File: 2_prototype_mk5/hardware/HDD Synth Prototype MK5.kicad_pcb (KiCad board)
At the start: 2 copper layers, 100.3 x 69.9 mm, 40 parts, among them J1 Micro_SD_Card, J6 171825-4, J7 Conn_01x04_Pin, J8 Conn_01x05, Q1 2N7002, U1 MAX98357A, U2 Optocoupler_DC_PhotoNPN_AKEC

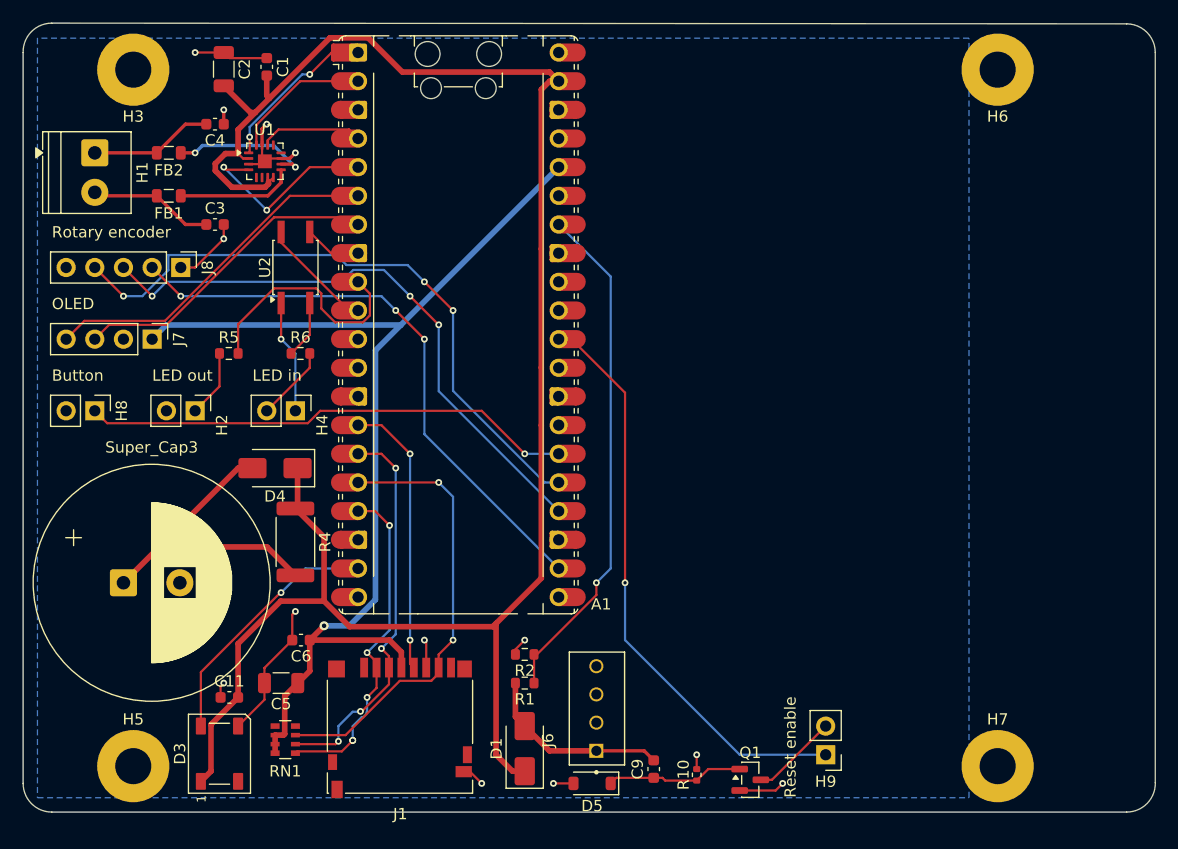
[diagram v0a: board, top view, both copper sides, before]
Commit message: MKV - SATA connector and wiring complete
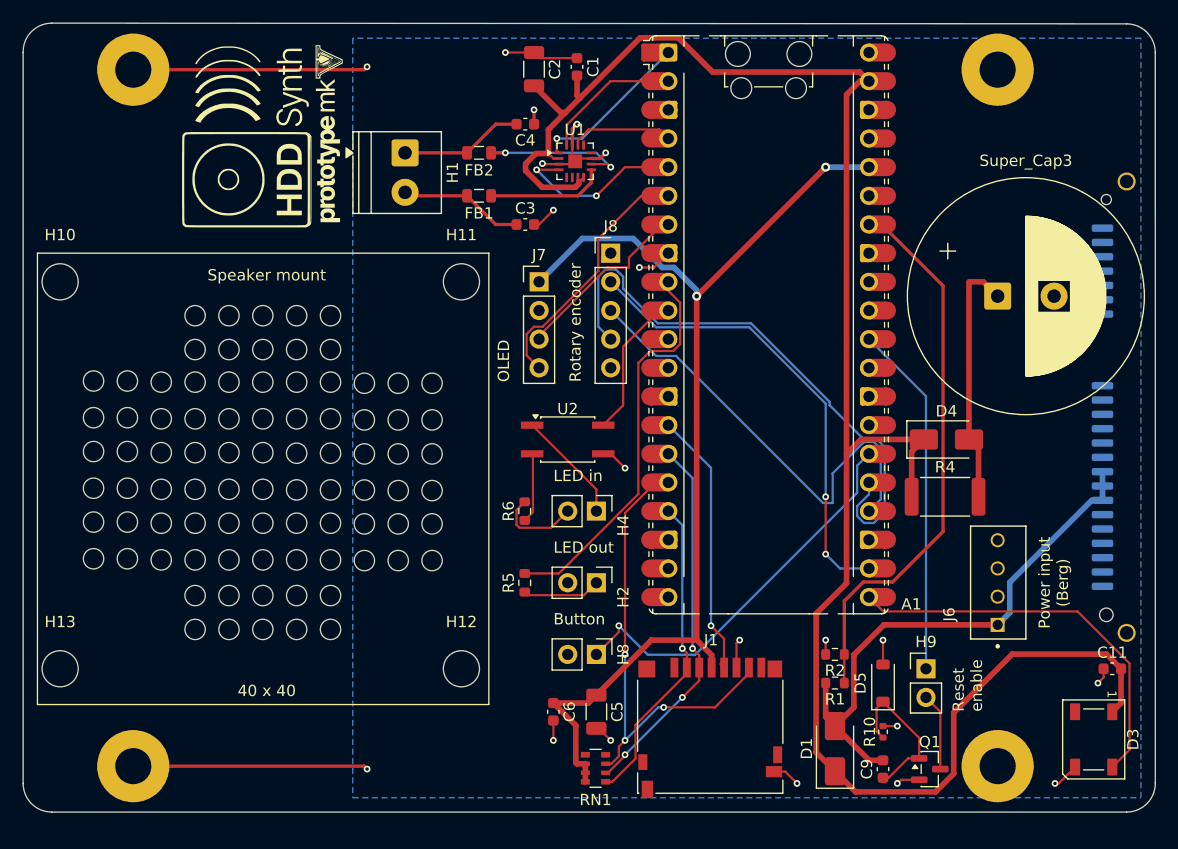
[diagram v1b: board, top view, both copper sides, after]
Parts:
- removed the G*** at (155.2, 79.3)
- added  : LOGO, HDDSyncMKIII:MHDDLA_Sound_40mm, B.Cu at (94.0, 62.1)
- added G***: LOGO, Custom:HDDSynthLogoMKV_15mm, F.Cu at (95.2, 55.9)
- added G***: LOGO, HDDSyncMKIII:MHDDLA_GB_40mm, B.Cu at (119.4, 104.1)
- added H10: MountingHole, MountingHole:MountingHole_3.2mm_M3, F.Cu at (76.9, 69.8)
- added H11: MountingHole, MountingHole:MountingHole_3.2mm_M3, F.Cu at (112.5, 69.8)
- added H12: MountingHole, MountingHole:MountingHole_3.2mm_M3, F.Cu at (112.5, 104.1)
- added H13: MountingHole, MountingHole:MountingHole_3.2mm_M3, F.Cu at (76.9, 104.1)
- added J2: SATA00102253A, Connector_SATA_SAS:SATA_Amphenol_10029364-001LF_Horizontal, B.Cu at (170.3, 81.0)
- moved Super_Cap3 81.5 mm to (160.0, 71.1)
- moved C11 78.3 mm to (170.2, 104.1)
- moved D3 77.5 mm to (168.5, 110.4), turned to -90 degrees
- moved D4 59.6 mm to (155.5, 83.8), turned to 0 degrees
- moved R4 57.7 mm to (155.4, 88.9), turned to 0 degrees
- moved H8 49.4 mm to (124.5, 102.9)
- moved H2 38.7 mm to (124.5, 96.5)
- moved J8 38.1 mm to (125.7, 67.3), turned to 0 degrees
- moved J6 37.3 mm to (160.0, 100.2)
- moved J7 34.7 mm to (119.4, 69.8), turned to 0 degrees
- moved R5 33.2 mm to (118.1, 96.5), turned to 90 degrees
- moved U2 28.5 mm to (121.9, 83.8), turned to 0 degrees
- moved H4 28.1 mm to (124.5, 90.2)
- moved C5 28.1 mm to (124.5, 108.0), turned to -90 degrees
- moved RN1 27.6 mm to (124.4, 113.0)
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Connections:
- A1 pad 19: /RGB LED/RGB_DATA -> unconnected-(A1-GPIO14-Pad19)_1
- A1 pad 21: unconnected-(A1-GPIO16-Pad21)_1 -> /RGB LED/RGB_DATA
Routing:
- net GND: track 54.1 -> 86.0 mm, vias 13 -> 20
- net +5V: track 16.8 -> 48.5 mm
- net /Reset/PICO_RUN: track 51.8 -> 31.3 mm, vias 1 -> 0
- net /HDD_LED_OUT: track 21.3 -> 35.3 mm
- net /RGB LED/RGB_DATA: track 22.5 -> 35.3 mm, vias 1 -> 0
- net /Rotary encoder/ENC_B: track 52.9 -> 41.0 mm, vias 3 -> 0
- net /OLED/OLED_SCL: track 28.1 -> 17.2 mm
- net /Rotary encoder/ENC_A: track 52.0 -> 41.2 mm, vias 3 -> 2
- net /OLED/OLED_SDA: track 31.1 -> 22.8 mm
- net /ACTION_BTN: track 43.6 -> 35.4 mm
- net Net-(D4-A): track 28.7 -> 22.4 mm
- net /Rotary encoder/ENC_SWITCH: track 57.0 -> 51.2 mm, vias 3 -> 0
- net /VCC_DETECT: track 45.5 -> 49.2 mm, vias 1 -> 0
- net /SD card reader/SD_MOSI: track 36.0 -> 33.0 mm, vias 4 -> 3
- net /SD card reader/SD_CS: track 30.9 -> 28.0 mm, vias 5 -> 1
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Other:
- outline, holes or cut-outs redrawn
- board text added: "40 x 40"
- board text added: "Power input (Berg)"
- board text added: "Power input (SATA)"
- board text added: "Speaker mount"
- board text removed: "1+2: Device 0 2+3: Device 1"
- board text removed: "CompactFlash Edition"
